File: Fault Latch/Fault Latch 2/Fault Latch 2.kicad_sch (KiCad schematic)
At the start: 105 parts, among them K101 Fujitsu_FTR-LYAA005x, K102 Fujitsu_FTR-LYAA005x, K103 Fujitsu_FTR-LYAA005x, Q101 Q_NPN_BEC, Q102 Q_NPN_BEC, Q103 Q_NPN_BEC, Q104 Q_NPN_BEC, Q105 Q_NMOS_GSD, Q106 Q_NMOS_GSD, Q107 Q_PMOS_GSD, Q108 Q_PMOS_GSD, Q109 Q_NMOS_GDS, Q110 Q_NPN_BEC, Q111 Q_NPN_BEC, Q112 Q_NMOS_GSD, Q113 Q_PMOS_GSD, SW101 SW_Omron_B3FS, SW102 SW_Omron_B3FS, SW103 SW_Omron_B3FS, U101 SFH617A-1, U102 SFH617A-1, U103 SFH617A-1, U104 74AHC1G00, U105 74AHC1G00, U106 74AHC1G00, U107 74LS279, U108 641964-1, U109 SFH617A-1, U110 SFH617A-1, U111 641964-1, U112 641964-1, U113 641964-1, U114 641964-1, U115 641964-1, U116 641964-1, U117 74AHC1G00, U118 LM555xM, U119 74AHC1G00, U120 641964-1, U121 SFH617A-1, U122 641964-1

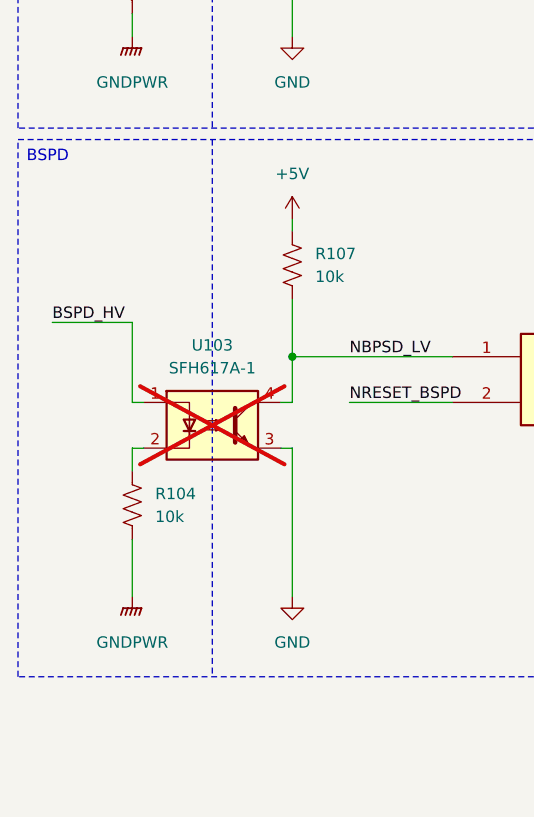
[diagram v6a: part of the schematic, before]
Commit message: BSPD now active low output, fault latch rerouted.
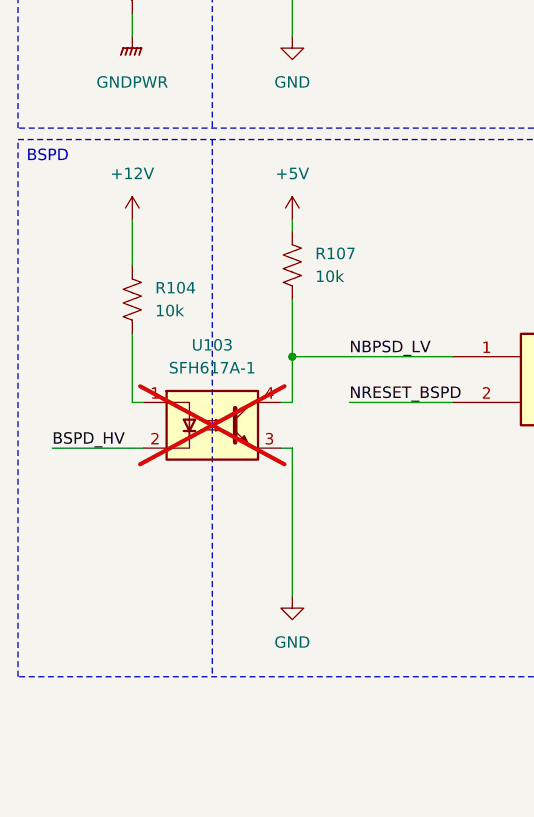
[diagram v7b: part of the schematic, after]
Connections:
- net +12V: now also R104.2
- net BSPD_HV: now also U103.2; no longer U103.1
- net GNDPWR: no longer R104.1
- new net: R104.1, U103.1
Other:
- moved on the sheet: R104
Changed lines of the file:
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@@
 	(wire
 		(pts
-			(xy 38.1 238.76) (xy 38.1 247.65)
-		)
-		(stroke
-			(width 0)
-			(type default)
-		)
-	)
-	(wire
-		(pts
 			(xy 317.5 311.15) (xy 309.88 311.15)
 		)
@@
 	(wire
 		(pts
-			(xy 38.1 252.73) (xy 39.37 252.73)
-		)
-		(stroke
-			(width 0)
-			(type default)
-		)
-	)
-	(wire
-		(pts
 			(xy 107.95 59.69) (xy 114.3 59.69)
 		)
@@
 	(wire
 		(pts
+			(xy 29.21 252.73) (xy 39.37 252.73)
+		)
+		(stroke
+			(width 0)
+			(type default)
+		)
+	)
+	(wire
+		(pts
 			(xy 209.55 95.25) (xy 209.55 96.52)
 		)
@@
 	(wire
 		(pts
-			(xy 29.21 238.76) (xy 38.1 238.76)
+			(xy 38.1 227.33) (xy 38.1 232.41)
 		)
 		(stroke
@@
 	(wire
 		(pts
-			(xy 38.1 255.27) (xy 38.1 252.73)
-		)
-		(stroke
-			(width 0)
-			(type default)
-		)
-	)
-	(wire
-		(pts
 			(xy 204.47 52.07) (xy 208.28 52.07)
 		)
@@
 	(wire
 		(pts
-			(xy 107.95 115.57) (xy 116.84 115.57)
+			(xy 38.1 240.03) (xy 38.1 247.65)
 		)
 		(stroke
@@
 	(wire
 		(pts
-			(xy 88.9 231.14) (xy 88.9 234.95)
+			(xy 107.95 115.57) (xy 116.84 115.57)
 		)
 		(stroke
@@
 	(wire
 		(pts
-			(xy 34.29 59.69) (xy 34.29 63.5)
+			(xy 88.9 231.14) (xy 88.9 234.95)
 		)
 		(stroke
@@
 	(wire
 		(pts
-			(xy 354.33 262.89) (xy 367.03 262.89)
+			(xy 34.29 59.69) (xy 34.29 63.5)
 		)
 		(stroke
@@
 	(wire
 		(pts
-			(xy 231.14 300.99) (xy 231.14 307.34)
+			(xy 354.33 262.89) (xy 367.03 262.89)
 		)
 		(stroke
@@
 	(wire
 		(pts
-			(xy 184.15 172.72) (xy 184.15 176.53)
+			(xy 231.14 300.99) (xy 231.14 307.34)
 		)
 		(stroke
@@
 	(wire
 		(pts
-			(xy 320.04 326.39) (xy 320.04 328.93)
+			(xy 184.15 172.72) (xy 184.15 176.53)
 		)
 		(stroke
@@
 	(wire
 		(pts
-			(xy 346.71 119.38) (xy 356.87 119.38)
+			(xy 320.04 326.39) (xy 320.04 328.93)
 		)
 		(stroke
@@
 	(wire
 		(pts
-			(xy 38.1 262.89) (xy 38.1 269.24)
+			(xy 346.71 119.38) (xy 356.87 119.38)
 		)
 		(stroke
@@
 	)
 	(label "BSPD_HV"
-		(at 29.21 238.76 0)
+		(at 29.21 252.73 0)
 		(effects
 			(font
@@
 	)
 	(symbol
+		(lib_id "power:+12V")
+		(at 38.1 227.33 0)
+		(unit 1)
+		(exclude_from_sim no)
+		(in_bom yes)
+		(on_board yes)
+		(dnp no)
+		(fields_autoplaced yes)
+		(property "Reference" "#PWR0175"
+			(at 38.1 231.14 0)
+			(effects
+				(font
+					(size 1.27 1.27)
+				)
+				(hide yes)
+			)
+		)
+		(property "Value" "+12V"
+			(at 38.1 222.25 0)
+			(effects
+				(font
+					(size 1.27 1.27)
+				)
+			)
+		)
+		(property "Footprint" ""
+			(at 38.1 227.33 0)
+			(effects
+				(font
+					(size 1.27 1.27)
+				)
+				(hide yes)
+			)
+		)
+		(property "Datasheet" ""
+			(at 38.1 227.33 0)
+			(effects
+				(font
+					(size 1.27 1.27)
+				)
+				(hide yes)
+			)
+		)
+		(property "Description" "Power symbol creates a global label with name \"+12V\""
+			(at 38.1 227.33 0)
+			(effects
+				(font
+					(size 1.27 1.27)
+				)
+				(hide yes)
+			)
+		)
+		(pin "1"
+		)
+		(instances
+			(project "Fault Latch 2"
+				(path "/478dd61d-7d78-47ee-b0a2-413879fe7325"
+					(reference "#PWR0175")
+					(unit 1)
+				)
+			)
+		)
+	)
+	(symbol
 		(lib_id "CONNECTOR:641964-1")
 		(at 151.13 308.61 180)
@@
 	(symbol
 		(lib_id "Device:R_US")
-		(at 38.1 259.08 180)
+		(at 38.1 236.22 180)
 		(unit 1)
 		(exclude_from_sim no)
@@
 		(dnp no)
 		(property "Reference" "R104"
-			(at 40.64 257.8099 0)
+			(at 40.64 234.9499 0)
 			(effects
 				(font
@@
 		)
 		(property "Value" "10k"
-			(at 40.64 260.3499 0)
+			(at 40.64 237.4899 0)
 			(effects
 				(font
@@
 		)
 		(property "Footprint" "Resistor_SMD:R_0805_2012Metric_Pad1.20x1.40mm_HandSolder"
-			(at 37.084 258.826 90)
+			(at 37.084 235.966 90)
 			(effects
 				(font
@@
 		)
 		(property "Datasheet" "~"
-			(at 38.1 259.08 0)
+			(at 38.1 236.22 0)
 			(effects
 				(font
@@
 		)
 		(property "Description" "Resistor, US symbol"
-			(at 38.1 259.08 0)
+			(at 38.1 236.22 0)
 			(effects
 				(font
@@
 		)
 		(property "JLC#" "C17414"
-			(at 38.1 259.08 0)
+			(at 38.1 236.22 0)
 			(effects
 				(font
@@
 		)
 		(property "Sim.Device" ""
-			(at 38.1 259.08 0)
+			(at 38.1 236.22 0)
 			(effects
 				(font
@@
 		)
 		(property "Sim.Pins" ""
-			(at 38.1 259.08 0)
+			(at 38.1 236.22 0)
 			(effects
 				(font
@@
 		)
 		(property "Sim.Type" ""
-			(at 38.1 259.08 0)
+			(at 38.1 236.22 0)
 			(effects
 				(font
@@
 		)
 		(property "MOUSER" ""
-			(at 38.1 259.08 0)
+			(at 38.1 236.22 0)
 			(effects
 				(font
@@
 		)
 		(property "Notes" ""
-			(at 38.1 259.08 0)
+			(at 38.1 236.22 0)
 			(effects
 				(font
@@
 					(unit 1)
 				)
-			)
-		)
-	)
-	(symbol
-		(lib_id "power:GNDPWR")
-		(at 38.1 269.24 0)
-		(unit 1)
-		(exclude_from_sim no)
-		(in_bom yes)
-		(on_board yes)
-		(dnp no)
-		(property "Reference" "#PWR0105"
-			(at 38.1 274.32 0)
-			(effects
-				(font
-					(size 1.27 1.27)
-				)
-				(hide yes)
-			)
-		)
-		(property "Value" "GNDPWR"
-			(at 38.1 274.32 0)
-			(effects
-				(font
-					(size 1.27 1.27)
-				)
-			)
-		)
-		(property "Footprint" ""
-			(at 38.1 270.51 0)
-			(effects
-				(font
-					(size 1.27 1.27)
-				)
-				(hide yes)
-			)
-		)
-		(property "Datasheet" ""
-			(at 38.1 270.51 0)
-			(effects
-				(font
-					(size 1.27 1.27)
-				)
-				(hide yes)
-			)
-		)
-		(property "Description" "Power symbol creates a global label with name \"GNDPWR\" , global ground"
-			(at 38.1 269.24 0)
-			(effects
-				(font
-					(size 1.27 1.27)
-				)
-				(hide yes)
-			)
-		)
-		(pin "1"
-		)
-		(instances
-			(project "Fault Latch 2"
-				(path "/478dd61d-7d78-47ee-b0a2-413879fe7325"
-					(reference "#PWR0105")
-					(unit 1)
-				)

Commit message: Updated BOM
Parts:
- K101, K102, K103: JLC# C1222376 -> (none); MOUSER (none) -> 817-FTR-LYAA005Y; Manufacturer_Part_Number (none) -> https://www.mouser.com/ProductDetail/FCL-Components/FTR-LYA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
- R102, R106, R107, R109, R121, R125, R126: JLC# C17590 -> (none); MOUSER (none) -> ESR10EZPD1002
- R112: value 500R -> 510R; JLC# C130232 -> (none); MOUSER (none) -> KTR03EZPF5100
- R130: JLC# C130232 -> (none); MOUSER (none) -> ESR03EZPF2700
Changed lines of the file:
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@@
 			)
 		)
-		(property "JLC#" "C1222376"
+		(property "JLC#" ""
 			(at 203.2 197.4849 0)
 			(effects
@@
 			)
 		)
-		(property "MOUSER" ""
+		(property "MOUSER" " 817-FTR-LYAA005Y "
 			(at 191.77 195.58 0)
 			(effects
@@
 			)
 		)
+		(property "Manufacturer_Part_Number" "https://www.mouser.com/ProductDetail/FCL-Components/FTR-LYAA005Y?qs=lEfYtVAeAoqtqRNkFkxQ7Q%3D%3D"
+			(at 191.77 195.58 0)
+			(effects
+				(font
+					(size 1.27 1.27)
+				)
+			)
+		)
 		(pin "A1"
 		)
@@
 			)
 		)
-		(property "JLC#" "C17590"
+		(property "JLC#" ""
 			(at 55.88 232.41 0)
 			(effects
@@
 			)
 		)
-		(property "MOUSER" ""
+		(property "MOUSER" "ESR10EZPD1002"
 			(at 55.88 232.41 0)
 			(effects
@@
 			)
 		)
-		(property "JLC#" "C17590"
+		(property "JLC#" ""
 			(at 157.48 323.85 0)
 			(effects
@@
 			)
 		)
-		(property "MOUSER" ""
+		(property "MOUSER" "ESR10EZPD1002"
 			(at 158.75 323.85 0)
 			(effects
@@
 			)
 		)
-		(property "JLC#" "C17590"
+		(property "JLC#" ""
 			(at 58.42 170.18 0)
 			(effects
@@
 			)
 		)
-		(property "MOUSER" ""
+		(property "MOUSER" "ESR10EZPD1002"
 			(at 58.42 170.18 0)
 			(effects
@@
 		(on_board yes)
 		(dnp no)
-		(fields_autoplaced yes)
 		(property "Reference" "R112"
-			(at 104.14 302.2599 0)
+			(at 104.648 296.926 0)
 			(effects
 				(font
@@
 			)
 		)
-		(property "Value" "500R"
-			(at 104.14 304.7999 0)
+		(property "Value" "510R"
+			(at 104.902 300.99 0)
 			(effects
 				(font
@@
 			)
 		)
-		(property "JLC#" "C130232"
+		(property "JLC#" ""
 			(at 101.6 303.53 0)
 			(effects
@@
 			)
 		)
+		(property "MOUSER" "KTR03EZPF5100 "
+			(at 101.6 303.53 0)
+			(effects
+				(font
+					(size 1.27 1.27)
+				)
+			)
+		)
 		(pin "2"
 		)
@@
 			)
 		)
-		(property "JLC#" "C1222376"
+		(property "JLC#" ""
 			(at 201.93 128.9049 0)
 			(effects
@@
 			)
 		)
-		(property "MOUSER" ""
+		(property "MOUSER" " 817-FTR-LYAA005Y "
 			(at 190.5 127 0)
 			(effects
@@
 			)
 		)
+		(property "Manufacturer_Part_Number" "https://www.mouser.com/ProductDetail/FCL-Components/FTR-LYAA005Y?qs=lEfYtVAeAoqtqRNkFkxQ7Q%3D%3D"
+			(at 190.5 127 0)
+			(effects
+				(font
+					(size 1.27 1.27)
+				)
+			)
+		)
 		(pin "A1"
 		)
@@
 			)
 		)
-		(property "JLC#" "C17590"
+		(property "JLC#" ""
 			(at 209.55 168.91 0)
 			(effects
@@
 			)
 		)
-		(property "MOUSER" ""
+		(property "MOUSER" "ESR10EZPD1002"
 			(at 210.82 168.91 0)
 			(effects
@@
 			)
 		)
-		(property "JLC#" "C17590"
+		(property "JLC#" ""
 			(at 38.1 115.57 0)
 			(effects
@@
 			)
 		)
-		(property "MOUSER" ""
+		(property "MOUSER" "ESR10EZPD1002"
 			(at 36.83 115.57 0)
 			(effects
@@
 			)
 		)
-		(property "JLC#" "C130232"
+		(property "JLC#" ""
 			(at 231.14 297.18 0)
 			(effects
@@
 			)
 		)
+		(property "MOUSER" "ESR03EZPF2700 "
+			(at 231.14 297.18 0)
+			(effects
+				(font
+					(size 1.27 1.27)
+				)
+			)
+		)
 		(pin "2"
 		)
@@
 			)
 		)
-		(property "JLC#" "C17590"
+		(property "JLC#" ""
 			(at 208.28 100.33 0)
 			(effects
@@
 			)
 		)
-		(property "MOUSER" ""
+		(property "MOUSER" "ESR10EZPD1002"
 			(at 209.55 100.33 0)
 			(effects
@@
 			)
 		)
-		(property "JLC#" "C1222376"
+		(property "JLC#" ""
 			(at 190.5 251.206 0)
 			(effects
@@
 			)
 		)
-		(property "MOUSER" ""
+		(property "MOUSER" " 817-FTR-LYAA005Y "
 			(at 190.5 247.65 0)
 			(effects
@@
 			)
 		)
+		(property "Manufacturer_Part_Number" "https://www.mouser.com/ProductDetail/FCL-Components/FTR-LYAA005Y?qs=lEfYtVAeAoqtqRNkFkxQ7Q%3D%3D"
+			(at 190.5 247.65 0)
+			(effects
+				(font
+					(size 1.27 1.27)
+				)
+			)
+		)
 		(pin "A1"
 		)
@@
 			)
 		)
-		(property "JLC#" "C17590"
+		(property "JLC#" ""
 			(at 54.61 105.41 0)
 			(effects
@@
 			)
 		)
-		(property "MOUSER" ""
+		(property "MOUSER" "ESR10EZPD1002"
 			(at 54.61 105.41 0)
 			(effects
